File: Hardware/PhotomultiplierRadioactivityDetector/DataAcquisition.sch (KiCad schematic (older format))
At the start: 43 parts, among them J1 Conn_01x04, J2 Conn_02x05_Counter_Clockwise, Q1 2N7002, Q2 Q_NPN_BEC, U1 Opamp_Dual_Generic, U2 MCP3425A0T-ECH, U3 MCP3425A0T-ECH, U4 STM8S003F3P

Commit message: initial version rework
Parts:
- removed C2: 10u, Capacitor_Tantalum_SMD:CP_EIA-3528-21_Kemet-B, symbol Device:CP
- removed C6: 100n, Capacitor_SMD:C_0805_2012Metric_Pad1.15x1.40mm_HandSolder, symbol Device:C
- removed C7: 10n, Capacitor_SMD:C_0805_2012Metric_Pad1.15x1.40mm_HandSolder, symbol Device:C
- removed C8: 680n, Capacitor_SMD:C_0805_2012Metric_Pad1.15x1.40mm_HandSolder, symbol Device:C
- removed D2: yellow, LED_SMD:LED_0805_2012Metric, symbol Device:LED
- removed D3: 0R resistor, Diode_SMD:D_MiniMELF, symbol Device:D
- removed D4: green, LED_SMD:LED_0805_2012Metric, symbol Device:LED
- removed D5: red, LED_SMD:LED_0805_2012Metric, symbol Device:LED
- removed J1: Conn_01x04, Connector_PinSocket_2.54mm:PinSocket_1x04_P2.54mm_Horizontal, symbol Connector_Generic:Conn_01x04
- removed J2: Conn_02x05_Counter_Clockwise, Connector_PinSocket_2.54mm:PinSocket_2x05_P2.54mm_Horizontal, symbol Connector_Generic:Conn_02x05_Counter_Clockwise
- removed R14: 510R, Resistor_SMD:R_0805_2012Metric_Pad1.15x1.40mm_HandSolder, symbol Device:R
- removed RV1: R_POT_TRIM, Potentiometer_THT:Potentiometer_Bourns_3296W_Vertical, symbol Device:R_POT_TRIM
- removed TP1, TP2, TP3, TP4, TP5, TP6: TestPoint, TestPoint:TestPoint_THTPad_1.0x1.0mm_Drill0.5mm, symbol Connector:TestPoint
- removed U1: Opamp_Dual_Generic, Package_SO:SOIC-8_3.9x4.9mm_P1.27mm, symbol Device:Opamp_Dual_Generic
- removed U2: MCP3425A0T-ECH, Package_TO_SOT_SMD:SOT-23-6_Handsoldering, symbol Analog_ADC:MCP3425A0T-ECH
- removed U4: STM8S003F3P, Package_SO:TSSOP-20_4.4x6.5mm_P0.65mm, symbol MCU_ST_STM8:STM8S003F3P
- added C2: 10n, Capacitor_SMD:C_0805_2012Metric_Pad1.15x1.40mm_HandSolder, symbol Device:C
- added D2, D6: 1n148, Diode_SMD:D_MiniMELF, symbol Device:D
- added R35, R36: 10k, Resistor_SMD:R_0805_2012Metric_Pad1.15x1.40mm_HandSolder, symbol Device:R
- added Rel1: RSM850B-6112-85-1005, Relay_THT:Relay_DPDT_Omron_G6K-2P-Y, symbol PhotomultiplierRadioactivityDetector:RSM850B-6112-85-1005
- added U1, U4: TL074, Package_SO:SOIC-14_3.9x8.7mm_P1.27mm, symbol Amplifier_Operational:TL074
- C1, C9: value 100n -> 10n
- Q2: footprint Package_TO_SOT_SMD:SOT-323_SC-70_Handsoldering -> Package_TO_SOT_SMD:SOT-323_SC-70
- R10: value 2k2 -> 1k
- R11: value 2k2 -> 10k
- R12, R13: value 510R -> 0R
- R2, R7: value 0R -> 10k
- R3: value 27k -> 10k
- R4, R5, R8, R9: value 1k -> 10k
- R6: value 0R -> 100R
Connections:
- net labels added: +9V, DIRECT_VOLTAGE, PEAK_VOLTAGE
- net labels removed: INT0, RST, RX, SWIM, TX, VCCIO, VCC_5V, VCC_PROG
- wire segments 155 -> 116
- no-connect marks 7 -> 0
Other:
- note added: "Dynode signal amilifier and conditionning"
- note added: "Peak detector"
- note removed: "TODO: \n1) rework input amplifier\n2) fix peak detector"
- moved on the sheet: C4, C5, D1, Q1, R1, U3

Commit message: draft of hw power supply
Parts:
- renumbered C9 to C1, C1 to C2, C2 to C3, C3 to C4, C4 to C5, C5 to C6, D6 to D2, D2 to D3, R4 to R1, R36 to R10, R1 to R11, R10 to R12, R11 to R13, R12 to R14, R13 to R15, R5 to R2, R8 to R3, R2 to R4, R3 to R5, R9 to R6, R6 to R7, R35 to R8, R7 to R9, U4 to U1, U4 to U2, U1 to U2

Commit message: draft of amplifier
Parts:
- removed C1: 10n, Capacitor_SMD:C_0805_2012Metric_Pad1.15x1.40mm_HandSolder, symbol Device:C
- removed C4: 100n, Capacitor_SMD:C_0805_2012Metric_Pad1.15x1.40mm_HandSolder, symbol Device:C
- removed R1, R10, R2, R3, R6, R8: 10k, Resistor_SMD:R_0805_2012Metric_Pad1.15x1.40mm_HandSolder, symbol Device:R
- removed unit 3 of U1
- removed unit 4 of U1
- removed unit 5 of U1
- removed U2: TL074, Package_SO:SOIC-14_3.9x8.7mm_P1.27mm, symbol Amplifier_Operational:TL074
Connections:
- wire segments 116 -> 79
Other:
- note removed: "Dynode signal amilifier and conditionning"

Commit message: add element,, footprint and 3d model for transformer
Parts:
- removed C3: 10n, Capacitor_SMD:C_0805_2012Metric_Pad1.15x1.40mm_HandSolder, symbol Device:C
- removed D3: 1n148, Diode_SMD:D_MiniMELF, symbol Device:D
- removed Q2: Q_NPN_BEC, Package_TO_SOT_SMD:SOT-323_SC-70, symbol Device:Q_NPN_BEC
- removed R12: 1k, Resistor_SMD:R_0805_2012Metric_Pad1.15x1.40mm_HandSolder, symbol Device:R
- removed R13: 10k, Resistor_SMD:R_0805_2012Metric_Pad1.15x1.40mm_HandSolder, symbol Device:R
- removed Rel1: RSM850B-6112-85-1005, Relay_THT:Relay_DPDT_Omron_G6K-2P-Y, symbol PhotomultiplierRadioactivityDetector:RSM850B-6112-85-1005
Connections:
- net labels removed: +9V, DIRECT_VOLTAGE, PEAK_VOLTAGE
- wire segments 79 -> 57
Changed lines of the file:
@@
 	3400 2300 3550 2300
-$Comp
-L Device:Q_NPN_BEC Q2
-U 1 1 5EF321C7
-P 6900 3450
-F 0 "Q2" H 7091 3496 50  0000 L CNN
-F 1 "Q_NPN_BEC" H 7091 3405 50  0000 L CNN
-F 2 "Package_TO_SOT_SMD:SOT-323_SC-70" H 7100 3550 50  0001 C CNN
-F 3 "~" H 6900 3450 50  0001 C CNN
-	1    6900 3450
-	1    0    0    -1
-$EndComp
-$Comp
-L PhotomultiplierRadioactivityDetector:RSM850B-6112-85-1005 Rel1
-U 1 1 5ED51FDC
-P 7300 2150
-F 0 "Rel1" H 7050 1250 50  0000 L CNN
-F 1 "RSM850B-6112-85-1005" H 7050 1150 50  0000 L CNN
-F 2 "Relay_THT:Relay_DPDT_Omron_G6K-2P-Y" H 7300 2150 50  0001 C CNN
-F 3 "" H 7300 2150 50  0001 C CNN
-	1    7300 2150
-	1    0    0    -1
-$EndComp
-$Comp
-L Device:D D3
-U 1 1 5ED53675
-P 6600 2750
-F 0 "D3" V 6554 2830 50  0000 L CNN
-F 1 "1n148" V 6645 2830 50  0000 L CNN
-F 2 "Diode_SMD:D_MiniMELF" H 6600 2750 50  0001 C CNN
-F 3 "~" H 6600 2750 50  0001 C CNN
-	1    6600 2750
-	0    1    1    0
-$EndComp
-$Comp
-L power:+9V #PWR08
-U 1 1 5ED54429
-P 7000 2300
-F 0 "#PWR08" H 7000 2150 50  0001 C CNN
-F 1 "+9V" H 7015 2473 50  0000 C CNN
-F 2 "" H 7000 2300 50  0001 C CNN
-F 3 "" H 7000 2300 50  0001 C CNN
-	1    7000 2300
-	1    0    0    -1
-$EndComp
-$Comp
-L Device:R R13
-U 1 1 5ED54B7C
-P 6550 3650
-F 0 "R13" H 6620 3696 50  0000 L CNN
-F 1 "10k" H 6620 3605 50  0000 L CNN
-F 2 "Resistor_SMD:R_0805_2012Metric_Pad1.15x1.40mm_HandSolder" V 6480 3650 50  0001 C CNN
-F 3 "~" H 6550 3650 50  0001 C CNN
-	1    6550 3650
-	1    0    0    -1
-$EndComp
-$Comp
-L Device:R R12
-U 1 1 5ED54FCF
-P 5950 3450
-F 0 "R12" V 6157 3450 50  0000 C CNN
-F 1 "1k" V 6066 3450 50  0000 C CNN
-F 2 "Resistor_SMD:R_0805_2012Metric_Pad1.15x1.40mm_HandSolder" V 5880 3450 50  0001 C CNN
-F 3 "~" H 5950 3450 50  0001 C CNN
-	1    5950 3450
-	0    -1   -1   0
-$EndComp
-$Comp
-L Device:C C3
-U 1 1 5ED553E2
-P 6200 3650
-F 0 "C3" H 6085 3604 50  0000 R CNN
-F 1 "10n" H 6085 3695 50  0000 R CNN
-F 2 "Capacitor_SMD:C_0805_2012Metric_Pad1.15x1.40mm_HandSolder" H 6238 3500 50  0001 C CNN
-F 3 "~" H 6200 3650 50  0001 C CNN
-	1    6200 3650
-	-1   0    0    1
-$EndComp
-$Comp
-L power:GND #PWR09
-U 1 1 5ED55B22
-P 7000 3850
-F 0 "#PWR09" H 7000 3600 50  0001 C CNN
-F 1 "GND" H 7005 3677 50  0000 C CNN
-F 2 "" H 7000 3850 50  0001 C CNN
-F 3 "" H 7000 3850 50  0001 C CNN
-	1    7000 3850
-	1    0    0    -1
-$EndComp
-Wire Wire Line
-	7000 3250 7000 3050
-Wire Wire Line
-	7000 3050 6600 3050
-Wire Wire Line
-	6600 3050 6600 2900
-Connection ~ 7000 3050
-Wire Wire Line
-	7000 3050 7000 3000
-Wire Wire Line
-	7000 2450 7000 2350
-Wire Wire Line
-	7000 2350 6600 2350
-Wire Wire Line
-	6600 2350 6600 2600
-Connection ~ 7000 2350
-Wire Wire Line
-	7000 2350 7000 2300
-Wire Wire Line
-	7000 3850 7000 3650
-Wire Wire Line
-	6100 3450 6200 3450
-Wire Wire Line
-	6550 3500 6550 3450
-Connection ~ 6550 3450
-Wire Wire Line
-	6550 3450 6700 3450
-Wire Wire Line
-	6200 3500 6200 3450
-Connection ~ 6200 3450
-Wire Wire Line
-	6200 3450 6550 3450
-$Comp
-L power:GND #PWR07
-U 1 1 5ED6AA34
-P 6550 3850
-F 0 "#PWR07" H 6550 3600 50  0001 C CNN
-F 1 "GND" H 6555 3677 50  0000 C CNN
-F 2 "" H 6550 3850 50  0001 C CNN
-F 3 "" H 6550 3850 50  0001 C CNN
-	1    6550 3850
-	1    0    0    -1
-$EndComp
-$Comp
-L power:GND #PWR06
-U 1 1 5ED6ACA2
-P 6200 3850
-F 0 "#PWR06" H 6200 3600 50  0001 C CNN
-F 1 "GND" H 6205 3677 50  0000 C CNN
-F 2 "" H 6200 3850 50  0001 C CNN
-F 3 "" H 6200 3850 50  0001 C CNN
-	1    6200 3850
-	1    0    0    -1
-$EndComp
-Wire Wire Line
-	6200 3850 6200 3800
-Wire Wire Line
-	6550 3850 6550 3800
 $Comp
 L Device:R R14
@@
 Wire Wire Line
 	8400 3050 8400 2250
-Wire Wire Line
-	8400 2250 7300 2250
-Wire Wire Line
-	7300 2250 7300 2450
-Wire Wire Line
-	7150 2450 7150 1850
-Wire Wire Line
-	7150 1850 6500 1850
-Wire Wire Line
-	7450 2450 7450 1700
-Wire Wire Line
-	7450 1700 6500 1700
-Text Label 6500 1700 2    50   ~ 0
-PEAK_VOLTAGE
-Text Label 6500 1850 2    50   ~ 0
-DIRECT_VOLTAGE
 $Comp
 L Amplifier_Operational:TL074 U1

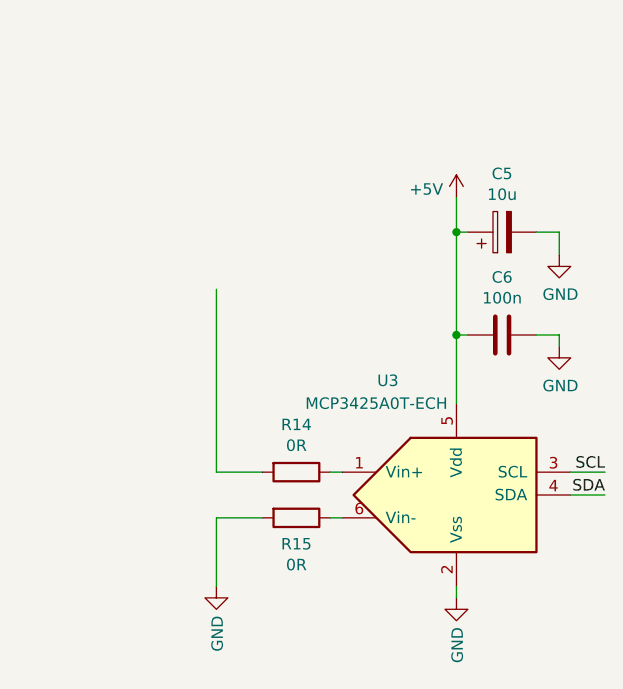
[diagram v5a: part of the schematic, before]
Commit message: draft of modules placement
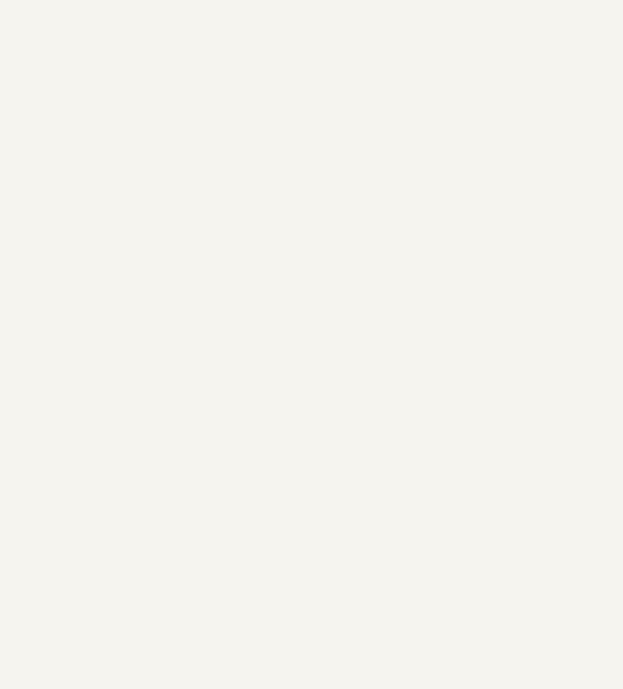
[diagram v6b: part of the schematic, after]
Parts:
- removed C5: 10u, Capacitor_Tantalum_SMD:CP_EIA-3528-21_Kemet-B, symbol Device:CP
- removed C6: 100n, Capacitor_SMD:C_0805_2012Metric_Pad1.15x1.40mm_HandSolder, symbol Device:C
- removed R14, R15: 0R, Resistor_SMD:R_0805_2012Metric_Pad1.15x1.40mm_HandSolder, symbol Device:R
- removed U3: MCP3425A0T-ECH, Package_TO_SOT_SMD:SOT-23-6_Handsoldering, symbol Analog_ADC:MCP3425A0T-ECH
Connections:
- net labels removed: +5V, SCL, SDA
- wire segments 57 -> 39
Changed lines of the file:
@@
-$EndComp
-$Comp
-L Analog_ADC:MCP3425A0T-ECH U3
-U 1 1 5CE375F5
-P 9450 3150
-F 0 "U3" H 9150 3650 50  0000 C CNN
-F 1 "MCP3425A0T-ECH" H 9100 3550 50  0000 C CNN
-F 2 "Package_TO_SOT_SMD:SOT-23-6_Handsoldering" H 9450 3150 50  0001 C CIN
-F 3 "http://ww1.microchip.com/downloads/en/DeviceDoc/22072b.pdf" H 9450 3150 50  0001 C CNN
-	1    9450 3150
-	1    0    0    -1
-$EndComp
-$Comp
-L Device:CP C5
-U 1 1 5CE37F43
-P 9650 2000
-F 0 "C5" V 9905 2000 50  0000 C CNN
-F 1 "10u" V 9814 2000 50  0000 C CNN
-F 2 "Capacitor_Tantalum_SMD:CP_EIA-3528-21_Kemet-B" H 9688 1850 50  0001 C CNN
-F 3 "~" H 9650 2000 50  0001 C CNN
-	1    9650 2000
-	0    -1   -1   0
 $EndComp
 $Comp
@@
 	0    -1   -1   0
 $EndComp
-$Comp
-L power:+5V #PWR013
-U 1 1 5CEC5BB5
-P 9450 1850
-F 0 "#PWR013" H 9450 1700 50  0001 C CNN
-F 1 "+5V" H 9392 1887 50  0000 R CNN
-F 2 "" H 9450 1850 50  0001 C CNN
-F 3 "" H 9450 1850 50  0001 C CNN
-	1    9450 1850
-	1    0    0    -1
-$EndComp
-$Comp
-L power:GND #PWR015
-U 1 1 5CEC60FD
-P 9900 2100
-F 0 "#PWR015" H 9900 1850 50  0001 C CNN
-F 1 "GND" H 9905 1927 50  0000 C CNN
-F 2 "" H 9900 2100 50  0001 C CNN
-F 3 "" H 9900 2100 50  0001 C CNN
-	1    9900 2100
-	1    0    0    -1
-$EndComp
-Wire Wire Line
-	9450 2000 9500 2000
-Wire Wire Line
-	9800 2000 9900 2000
-Wire Wire Line
-	9900 2000 9900 2100
-Wire Wire Line
-	9450 2000 9450 1850
-Connection ~ 9450 2000
-$Comp
-L power:GND #PWR014
-U 1 1 5CFAD0BC
-P 9450 3600
-F 0 "#PWR014" H 9450 3350 50  0001 C CNN
-F 1 "GND" V 9455 3472 50  0000 R CNN
-F 2 "" H 9450 3600 50  0001 C CNN
-F 3 "" H 9450 3600 50  0001 C CNN
-	1    9450 3600
-	1    0    0    -1
-$EndComp
-Wire Wire Line
-	9450 3600 9450 3550
 Text GLabel 800  1850 1    50   Input ~ 0
 analog_output
-Wire Wire Line
-	9950 3050 10100 3050
-Wire Wire Line
-	9950 3150 10100 3150
-Text Label 10100 3050 2    50   ~ 0
-SCL
-Text Label 10100 3150 2    50   ~ 0
-SDA
 Text Label 4250 2300 0    50   ~ 0
 RST_PEAK
-Wire Wire Line
-	9900 2450 9900 2500
-Wire Wire Line
-	9800 2450 9900 2450
-Wire Wire Line
-	9450 2450 9450 2000
-Connection ~ 9450 2450
-Wire Wire Line
-	9500 2450 9450 2450
-Wire Wire Line
-	9450 2750 9450 2450
-$Comp
-L power:GND #PWR016
-U 1 1 5CEC6490
-P 9900 2500
-F 0 "#PWR016" H 9900 2250 50  0001 C CNN
-F 1 "GND" H 9905 2327 50  0000 C CNN
-F 2 "" H 9900 2500 50  0001 C CNN
-F 3 "" H 9900 2500 50  0001 C CNN
-	1    9900 2500
-	1    0    0    -1
-$EndComp
-$Comp
-L Device:C C6
-U 1 1 5CE37B6C
-P 9650 2450
-F 0 "C6" V 9398 2450 50  0000 C CNN
-F 1 "100n" V 9489 2450 50  0000 C CNN
-F 2 "Capacitor_SMD:C_0805_2012Metric_Pad1.15x1.40mm_HandSolder" H 9688 2300 50  0001 C CNN
-F 3 "~" H 9650 2450 50  0001 C CNN
-	1    9650 2450
-	0    1    1    0
-$EndComp
 $Comp
 L Device:D D2
@@
 	3400 2300 3550 2300
 $Comp
-L Device:R R14
-U 1 1 5ED790F7
-P 8750 3050
-F 0 "R14" V 8543 3050 50  0000 C CNN
-F 1 "0R" V 8634 3050 50  0000 C CNN
-F 2 "Resistor_SMD:R_0805_2012Metric_Pad1.15x1.40mm_HandSolder" V 8680 3050 50  0001 C CNN
-F 3 "~" H 8750 3050 50  0001 C CNN
-	1    8750 3050
-	0    1    1    0
-$EndComp
-$Comp
-L Device:R R15
-U 1 1 5ED79958
-P 8750 3250
-F 0 "R15" V 8865 3250 50  0000 C CNN
-F 1 "0R" V 8956 3250 50  0000 C CNN
-F 2 "Resistor_SMD:R_0805_2012Metric_Pad1.15x1.40mm_HandSolder" V 8680 3250 50  0001 C CNN
-F 3 "~" H 8750 3250 50  0001 C CNN
-	1    8750 3250
-	0    1    1    0
-$EndComp
-$Comp
-L power:GND #PWR012
-U 1 1 5ED79DB5
-P 8400 3550
-F 0 "#PWR012" H 8400 3300 50  0001 C CNN
-F 1 "GND" V 8405 3422 50  0000 R CNN
-F 2 "" H 8400 3550 50  0001 C CNN
-F 3 "" H 8400 3550 50  0001 C CNN
-	1    8400 3550
-	1    0    0    -1
-$EndComp
-Wire Wire Line
-	8950 3250 8900 3250
-Wire Wire Line
-	8600 3250 8400 3250
-Wire Wire Line
-	8400 3250 8400 3550
-Wire Wire Line
-	8950 3050 8900 3050
-Wire Wire Line
-	8600 3050 8400 3050
-Wire Wire Line
-	8400 3050 8400 2250
-$Comp
 L Amplifier_Operational:TL074 U1

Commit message: improve component placement
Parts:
- added C18, C42, C43, C5, C6: 100n, Capacitor_SMD:C_0805_2012Metric_Pad1.15x1.40mm_HandSolder, symbol Device:C
- added L1, L2, L3, L4: L, Inductor_SMD:L_0805_2012Metric, symbol Device:L
- added Q2, Q7: Q_NJFET_DGS, Package_TO_SOT_SMD:SC-59, symbol Device:Q_NJFET_DGS
- added R15, R22, R35, R59, R60: 10k, Resistor_SMD:R_0805_2012Metric_Pad1.15x1.40mm_HandSolder, symbol Device:R
- added U3: TL074, Package_SO:SOIC-14_3.9x8.7mm_P1.27mm, symbol Amplifier_Operational:TL074
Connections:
- net labels added: VCC
- wire segments 39 -> 82
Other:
- moved on the sheet: C2, D1, D2, Q1, R11, R4, R5, R7, R9, U1A, U1B
